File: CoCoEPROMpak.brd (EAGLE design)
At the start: 53.3 x 44.5 mm, 5 parts, among them P1 COCO-CART, U1 2732, U2 27128

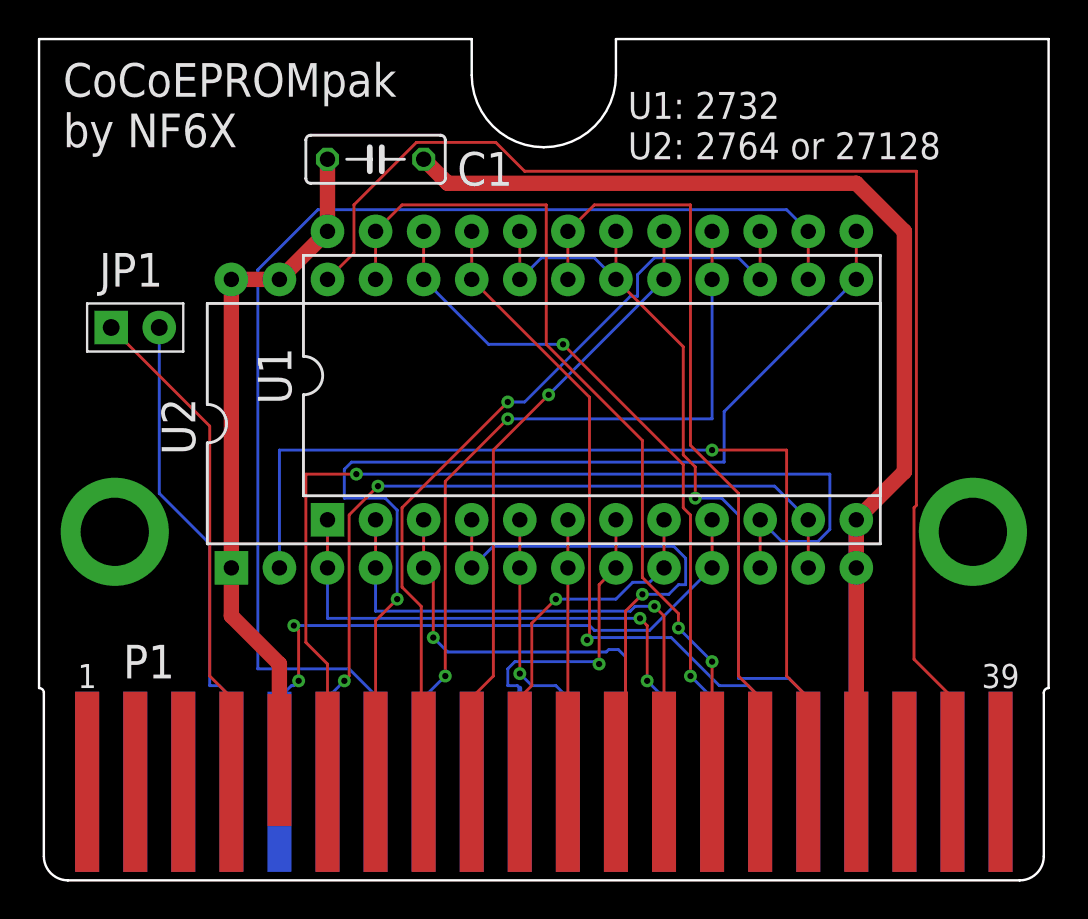
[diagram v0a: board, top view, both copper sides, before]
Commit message: Added support for 27256 and 27512 EPROMs with bank-switching by jumper settings.
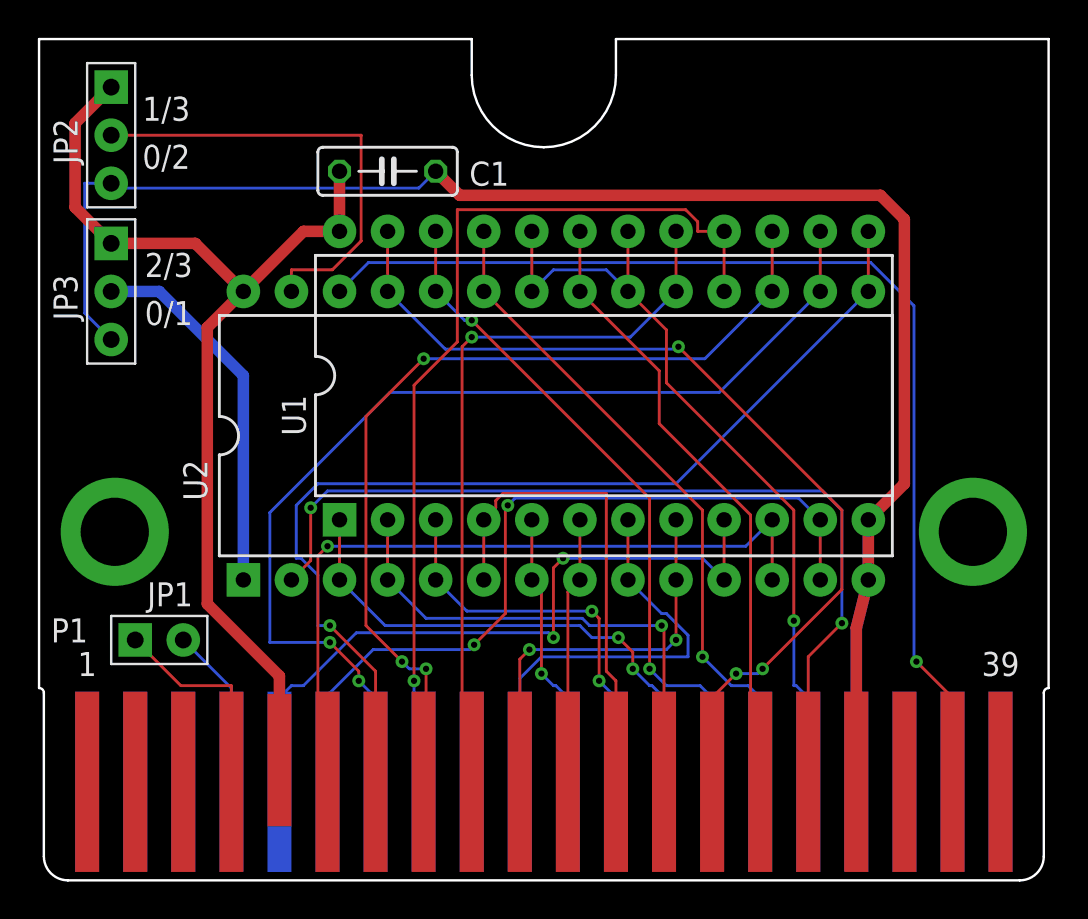
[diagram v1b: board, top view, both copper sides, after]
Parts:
- added JP2, JP3: JP3, switch:JP3-100MIL
- U2: value 27128 -> 27512
- moved JP1 16.6 mm to (5.08, 12.7)
- moved C1 0.90 mm to (18.4, 37.5)
- moved U2 0.90 mm to (27.3, 23.5)
- moved U1 0.63 mm to (29.8, 26.7)
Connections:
- new net N$1: JP2.2, U2.27
- new net N$3: JP3.2, U2.1
- net +5V: now also JP2.1, JP3.1; no longer U2.1, U2.27
- net GND: now also JP2.3, JP3.3
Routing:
- net GND: track 71.0 -> 98.2 mm
- net N$1: track 0.00 -> 24.3 mm
- net N$3: track 0.00 -> 19.6 mm
- net +5V: track 36.4 -> 54.6 mm
- net N$4: track 25.9 -> 8.55 mm
- net N$5: track 26.6 -> 11.2 mm
- net D1: track 54.3 -> 40.1 mm
- net A13: track 69.4 -> 58.0 mm, vias 0 -> 1
- net D4: track 65.9 -> 55.5 mm, vias 0 -> 2
- net A10: track 41.6 -> 33.0 mm
- net D6: track 41.7 -> 49.7 mm, vias 2 -> 1
- net D7: track 33.3 -> 38.9 mm
- net D5: track 43.0 -> 48.6 mm, vias 1 -> 3
- net A1: track 19.6 -> 23.5 mm, vias 1 -> 0
- net A8: track 46.2 -> 49.9 mm, vias 2 -> 3
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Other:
- board text added: "0/1"
- board text added: "0/2"
- board text added: "1/3"
- board text added: "2/3"
- board text removed: "U1: 2732 U2: 2764 or 27128"

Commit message: Documentation improvements.
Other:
- board text added: "A14/!PGM!: 1 0"
- board text added: "A15/VPP: 1 0"
- board text added: "AUTOSTART"
- board text removed: "0/1"
- board text removed: "0/2"
- board text removed: "1/3"
- board text removed: "2/3"
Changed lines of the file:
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@@
 Distributed under GPLv3
 https://github.com/NF6X/CoCoEPROMpak</text>
-<text x="5.588" y="29.337" size="1.27" layer="21" font="vector">0/1</text>
-<text x="5.588" y="31.877" size="1.27" layer="21" font="vector">2/3</text>
-<text x="5.461" y="37.592" size="1.27" layer="21" font="vector">0/2</text>
-<text x="5.461" y="40.132" size="1.27" layer="21" font="vector">1/3</text>
+<text x="5.588" y="29.337" size="1.27" layer="21" font="vector">A15/VPP:
+1
+0</text>
+<text x="5.461" y="37.592" size="1.27" layer="21" font="vector">A14/!PGM!:
+1
+0</text>
 <text x="31.75" y="38.1" size="1.778" layer="29" font="vector">CoCoEPROMpak
 by NF6X</text>
+<text x="9.525" y="12.065" size="1.27" layer="21" font="vector">AUTOSTART</text>
 </plain>
 <attributes>
@@
 </class>
 </classes>
-<designrules name="LaenPCBOrder">
+<designrules name="LaenPCBOrder *">
 <description language="de">&lt;b&gt;EAGLE Design Rules&lt;/b&gt;
 &lt;p&gt;
@@
 <param name="mlMinCreamFrame" value="0mil"/>
 <param name="mlMaxCreamFrame" value="0mil"/>
-<param name="mlViaStopLimit" value="0mil"/>
+<param name="mlViaStopLimit" value="25mil"/>
 <param name="srRoundness" value="0"/>
 <param name="srMinRoundness" value="0mil"/>
